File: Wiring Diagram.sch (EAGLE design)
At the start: 36 parts, among them SW1 ENCODER_SW1-PEC12, SW2 ENCODER_SW1-PEC12, SW3 ENCODER_SW1-PEC12, SW4 ENCODER_SW1-PEC12

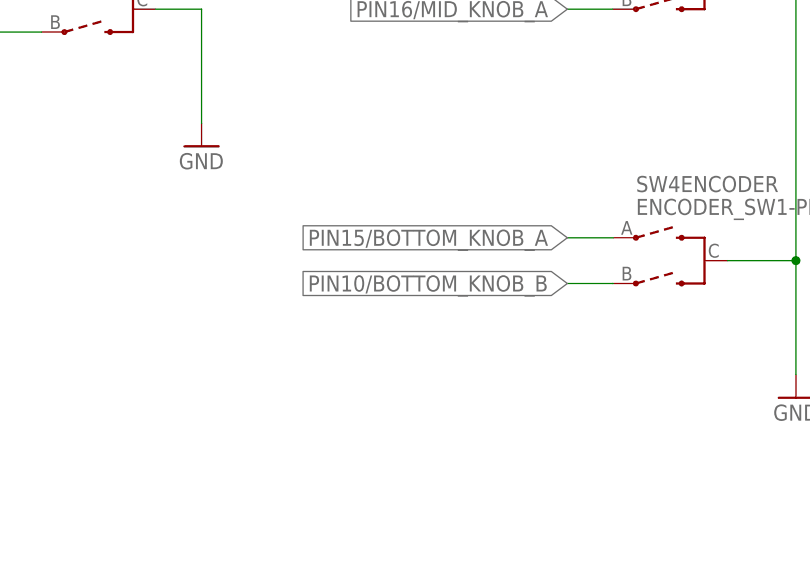
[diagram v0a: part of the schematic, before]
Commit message: Fixed error in wiring diagram
BOTTOM_KNOB_B was labeled as Pin 10, should be Pin 14. Thanks to @CarlesM on Twitter for spotting.
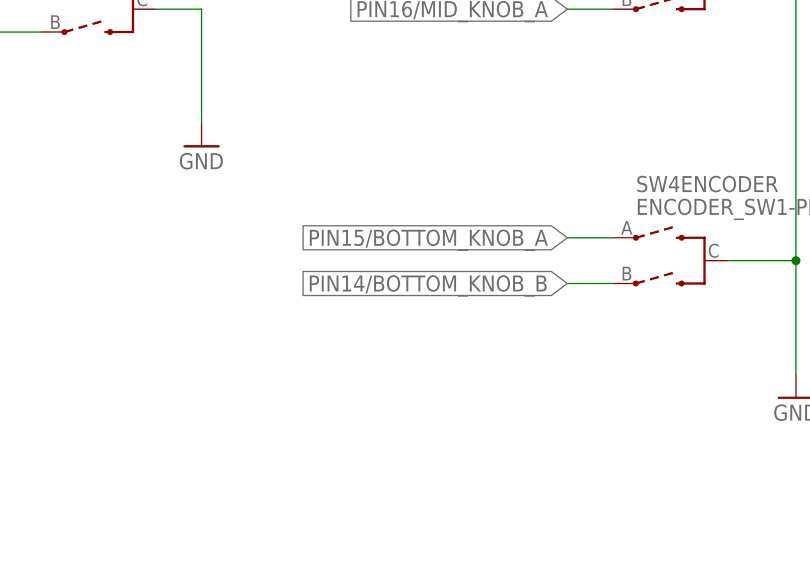
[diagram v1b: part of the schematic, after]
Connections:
- net PIN10/BOTTOM_KNOB_B renamed PIN14/BOTTOM_KNOB_B
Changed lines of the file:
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@@
 </segment>
 </net>
-<net name="PIN10/BOTTOM_KNOB_B" class="0">
+<net name="PIN14/BOTTOM_KNOB_B" class="0">
 <segment>
 <pinref part="SW4" gate="ENCODER" pin="B"/>
